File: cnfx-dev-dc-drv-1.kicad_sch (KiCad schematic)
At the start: 55 parts, among them J1 TC2030, J2 Conn_01x02, J3 Conn_01x04_Pin, J4 Conn_01x02, J7 Conn_01x03, J8 Conn_01x04_Pin, SW1 SW_Push, SW2 SW_Push, SW3 SW_Push, U1 SN65HVD230, U2 STM32F103C8Tx, U5 HT753-1, U6 TPS259472A, Y1 8M

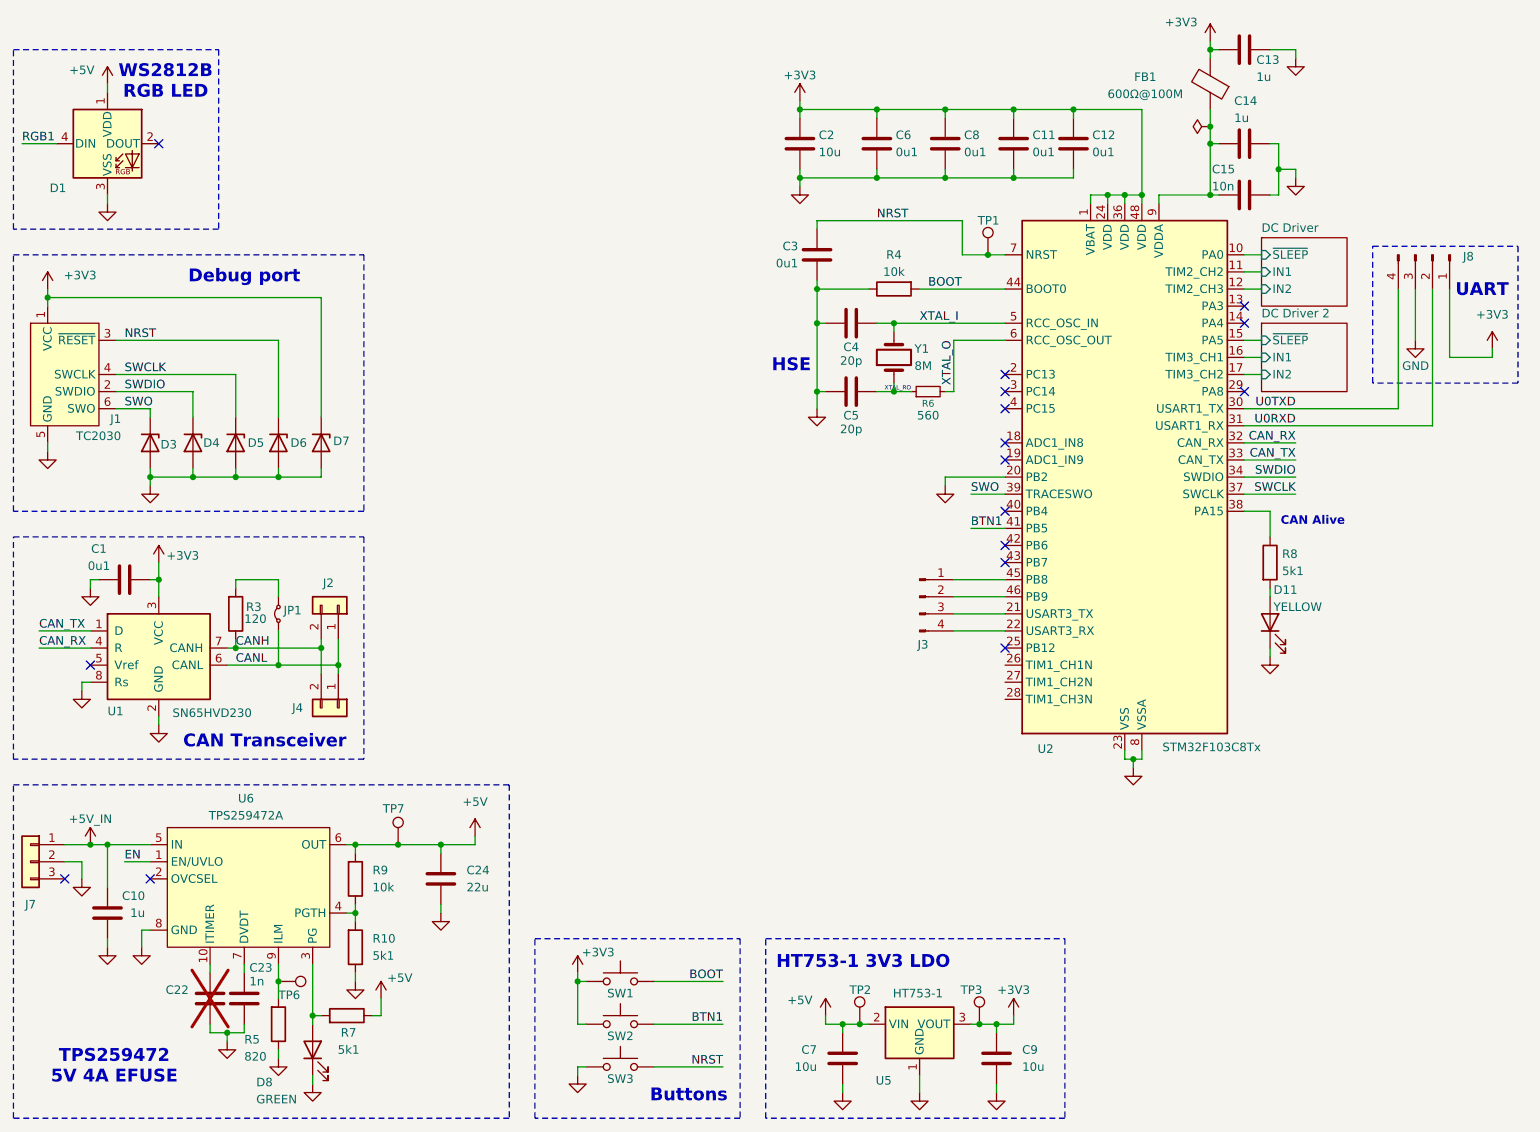
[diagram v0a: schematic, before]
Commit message: schem: connect rgb pin to stm32
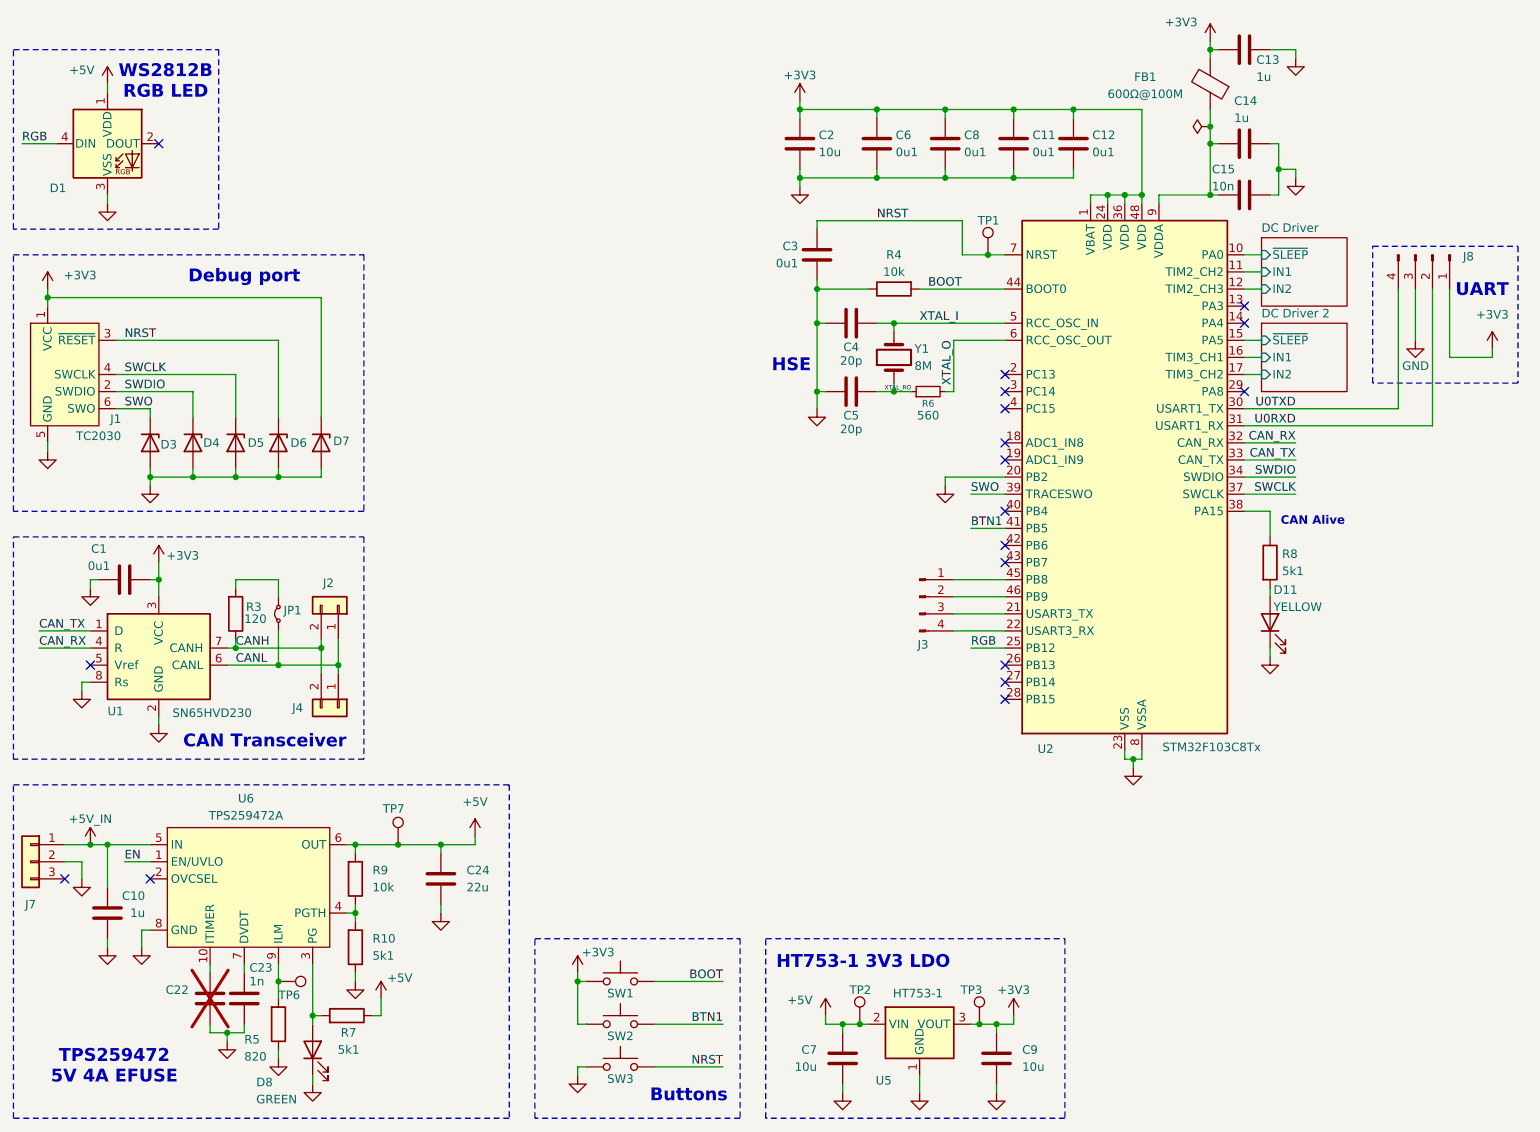
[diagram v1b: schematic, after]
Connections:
- net RGB1 is gone; now on net RGB: D1.4 (DIN)
- net RGB: now reaches U2.25 (PB12)
- no-connect marks 16 -> 18
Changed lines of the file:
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@@
 	)
 	(no_connect
+		(at 163.83 127)
+	)
+	(no_connect
 		(at 36.83 158.75)
 	)
@@
 	)
 	(no_connect
+		(at 163.83 129.54)
+	)
+	(no_connect
 		(at 163.83 93.98)
 	)
 	(no_connect
-		(at 163.83 124.46)
+		(at 163.83 132.08)
 	)
 	(no_connect
@@
 	(wire
 		(pts
+			(xy 158.75 124.46) (xy 163.83 124.46)
+		)
+		(stroke
+			(width 0)
+			(type default)
+		)
+	)
+	(wire
+		(pts
 			(xy 43.18 86.36) (xy 43.18 90.17)
 		)
@@
 		)
 	)
-	(label "RGB1"
+	(label "RGB"
 		(at 17.78 49.53 0)
 		(effects
@@
 		)
 	)
+	(label "RGB"
+		(at 158.75 124.46 0)
+		(effects
+			(font
+				(size 1.27 1.27)
+			)
+			(justify left bottom)
+		)
+	)
 	(label "NRST"
 		(at 144.78 60.96 0)
@@
 		)
 		(pin "27"
-			(alternate "TIM1_CH2N")
 		)
 		(pin "40"
@@
 		)
 		(pin "28"
-			(alternate "TIM1_CH3N")
 		)
 		(pin "30"
@@
 		)
 		(pin "26"
-			(alternate "TIM1_CH1N")
 		)
 		(pin "18"

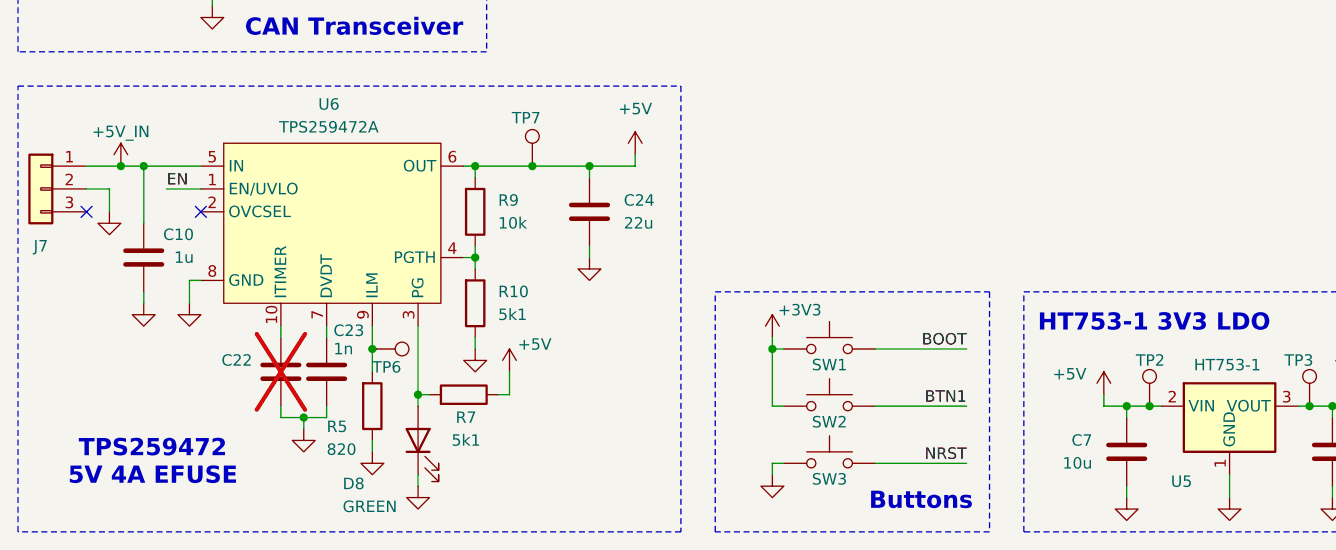
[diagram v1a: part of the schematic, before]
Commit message: schem: fix efuse en pin
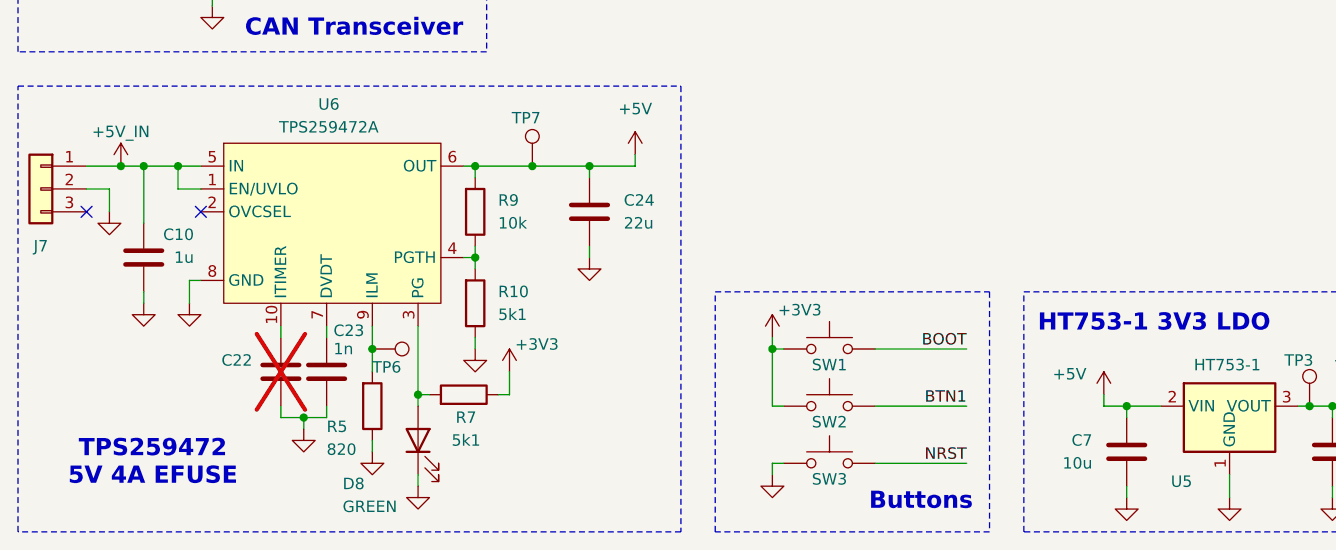
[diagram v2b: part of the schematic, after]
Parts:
- removed TP2: TestPoint, TestPoint:TestPoint_Pad_D2.0mm, symbol Connector:TestPoint
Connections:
- net EN is gone; now on net +5V_IN: U6.1 (EN/UVLO)
- net +3V3: now also R7.1
- net +5V: no longer R7.1
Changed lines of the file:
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@@
 	)
 	(junction
+		(at 34.29 153.67)
+		(diameter 0)
+		(color 0 0 0 0)
+	)
+	(junction
 		(at 62.23 124.46)
 		(diameter 0)
@@
 	)
 	(junction
-		(at 142.24 180.34)
-		(diameter 0)
-		(color 0 0 0 0)
-	)
-	(junction
 		(at 194.31 46.99)
 		(diameter 0)
@@
 	(wire
 		(pts
-			(xy 33.02 156.21) (xy 36.83 156.21)
-		)
-		(stroke
-			(width 0)
-			(type default)
-		)
-	)
-	(wire
-		(pts
 			(xy 195.58 57.15) (xy 194.31 57.15)
 		)
@@
 	(wire
 		(pts
+			(xy 34.29 156.21) (xy 34.29 153.67)
+		)
+		(stroke
+			(width 0)
+			(type default)
+		)
+	)
+	(wire
+		(pts
 			(xy 64.77 127) (xy 64.77 128.27)
 		)
@@
 	(wire
 		(pts
-			(xy 143.51 180.34) (xy 142.24 180.34)
-		)
-		(stroke
-			(width 0)
-			(type default)
-		)
-	)
-	(wire
-		(pts
 			(xy 30.48 153.67) (xy 30.48 160.02)
 		)
@@
 	(wire
 		(pts
+			(xy 34.29 156.21) (xy 36.83 156.21)
+		)
+		(stroke
+			(width 0)
+			(type default)
+		)
+	)
+	(wire
+		(pts
 			(xy 186.69 58.42) (xy 186.69 57.15)
 		)
@@
 	(wire
 		(pts
-			(xy 142.24 180.34) (xy 139.7 180.34)
+			(xy 139.7 180.34) (xy 143.51 180.34)
 		)
 		(stroke
@@
 	(wire
 		(pts
-			(xy 30.48 153.67) (xy 36.83 153.67)
+			(xy 30.48 153.67) (xy 34.29 153.67)
 		)
 		(stroke
@@
 	(wire
 		(pts
+			(xy 34.29 153.67) (xy 36.83 153.67)
+		)
+		(stroke
+			(width 0)
+			(type default)
+		)
+	)
+	(wire
+		(pts
 			(xy 207.01 93.98) (xy 199.39 93.98)
 		)
@@
 		)
 	)
-	(label "EN"
-		(at 33.02 156.21 0)
-		(effects
-			(font
-				(size 1.27 1.27)
-			)
-			(justify left bottom)
-		)
-	)
 	(label "CAN_RX"
 		(at 207.01 93.98 180)
@@
 	)
 	(symbol
+		(lib_id "power:+3V3")
+		(at 71.12 176.53 0)
+		(unit 1)
+		(body_style 1)
+		(exclude_from_sim no)
+		(in_bom yes)
+		(on_board yes)
+		(in_pos_files yes)
+		(dnp no)
+		(property "Reference" "#PWR044"
+			(at 71.12 180.34 0)
+			(hide yes)
+			(show_name no)
+			(do_not_autoplace no)
+			(effects
+				(font
+					(size 1.27 1.27)
+				)
+			)
+		)
+		(property "Value" "+3V3"
+			(at 74.168 173.482 0)
+			(show_name no)
+			(do_not_autoplace no)
+			(effects
+				(font
+					(size 1.27 1.27)
+				)
+			)
+		)
+		(property "Footprint" ""
+			(at 71.12 176.53 0)
+			(hide yes)
+			(show_name no)
+			(do_not_autoplace no)
+			(effects
+				(font
+					(size 1.27 1.27)
+				)
+			)
+		)
+		(property "Datasheet" ""
+			(at 71.12 176.53 0)
+			(hide yes)
+			(show_name no)
+			(do_not_autoplace no)
+			(effects
+				(font
+					(size 1.27 1.27)
+				)
+			)
+		)
+		(property "Description" "Power symbol creates a global label with name \"+3V3\""
+			(at 71.12 176.53 0)
+			(hide yes)
+			(show_name no)
+			(do_not_autoplace no)
+			(effects
+				(font
+					(size 1.27 1.27)
+				)
+			)
+		)
+		(pin "1"
+		)
+		(instances
+			(project "cnfx-dev-dc-drv-1"
+				(path "/d7250a19-615d-468e-abbc-0dea4b78aeef"
+					(reference "#PWR044")
+					(unit 1)
+				)
+			)
+		)
+	)
+	(symbol
 		(lib_id "power:GND")
 		(at 182.88 142.24 0)
@@
 	)
 	(symbol
-		(lib_id "Connector:TestPoint")
-		(at 142.24 180.34 0)
-		(unit 1)
-		(body_style 1)
-		(exclude_from_sim no)
-		(in_bom no)
-		(on_board yes)
-		(in_pos_files yes)
-		(dnp no)
-		(property "Reference" "TP2"
-			(at 140.716 175.26 0)
-			(show_name no)
-			(do_not_autoplace no)
-			(effects
-				(font
-					(size 1.27 1.27)
-				)
-				(justify left)
-			)
-		)
-		(property "Value" "TestPoint"
-			(at 144.78 178.3079 0)
-			(hide yes)
-			(show_name no)
-			(do_not_autoplace no)
-			(effects
-				(font
-					(size 1.27 1.27)
-				)
-				(justify left)
-			)
-		)
-		(property "Footprint" "TestPoint:TestPoint_Pad_D2.0mm"
-			(at 147.32 180.34 0)
-			(hide yes)
-			(show_name no)
-			(do_not_autoplace no)
-			(effects
-				(font
-					(size 1.27 1.27)
-				)
-			)
-		)
-		(property "Datasheet" ""
-			(at 147.32 180.34 0)
-			(hide yes)
-			(show_name no)
-			(do_not_autoplace no)
-			(effects
-				(font
-					(size 1.27 1.27)
-				)
-			)
-		)
-		(property "Description" "test point"
-			(at 142.24 180.34 0)
-			(hide yes)
-			(show_name no)
-			(do_not_autoplace no)
-			(effects
-				(font
-					(size 1.27 1.27)
-				)
-			)
-		)
-		(pin "1"
-		)
-		(instances
-			(project "cnfx-dev-dc-drv-1"
-				(path "/d7250a19-615d-468e-abbc-0dea4b78aeef"
-					(reference "TP2")
-					(unit 1)
-				)
-			)
-		)
-	)
-	(symbol
 		(lib_id "Connector:Conn_01x04_Pin")
 		(at 227.33 66.04 270)
@@
 					(unit 1)
 				)
-			)
-		)
-	)
-	(symbol
-		(lib_id "power:VBUS")
-		(at 71.12 176.53 0)
-		(unit 1)
-		(body_style 1)
-		(exclude_from_sim no)
-		(in_bom yes)
-		(on_board yes)
-		(in_pos_files yes)
-		(dnp no)
-		(property "Reference" "#PWR044"
-			(at 71.12 180.34 0)
-			(hide yes)
-			(show_name no)
-			(do_not_autoplace no)
-			(effects
-				(font
-					(size 1.27 1.27)
-				)
-			)
-		)
-		(property "Value" "+5V"
-			(at 73.914 173.482 0)
-			(show_name no)
-			(do_not_autoplace no)
-			(effects
-				(font
-					(size 1.27 1.27)
-				)
-			)
-		)
-		(property "Footprint" ""
-			(at 71.12 176.53 0)
-			(hide yes)
-			(show_name no)
-			(do_not_autoplace no)
-			(effects
-				(font
-					(size 1.27 1.27)
-				)
-			)
-		)
-		(property "Datasheet" ""
-			(at 71.12 176.53 0)
-			(hide yes)
-			(show_name no)
-			(do_not_autoplace no)
-			(effects
-				(font
-					(size 1.27 1.27)
-				)
-			)
-		)
-		(property "Description" "Power symbol creates a global label with name \"VBUS\""
-			(at 71.12 176.53 0)
-			(hide yes)
-			(show_name no)
-			(do_not_autoplace no)
-			(effects
-				(font
-					(size 1.27 1.27)
-				)
-			)
-		)
-		(pin "1"
-		)
-		(instances
-			(project "cnfx-dev-dc-drv-1"
-				(path "/d7250a19-615d-468e-abbc-0dea4b78aeef"
-					(reference "#PWR044")
-					(unit 1)
-				)

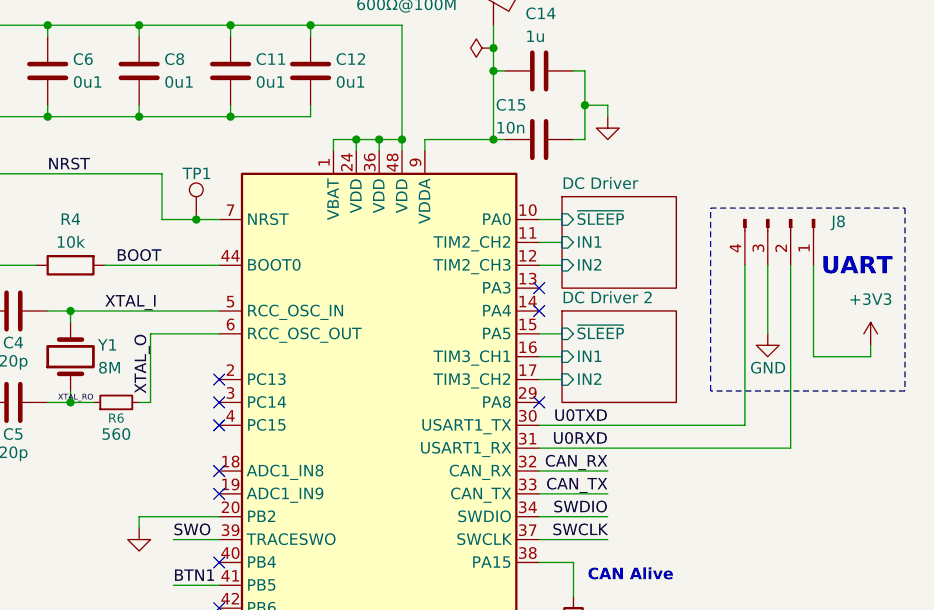
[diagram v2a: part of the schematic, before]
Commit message: schem: add test points
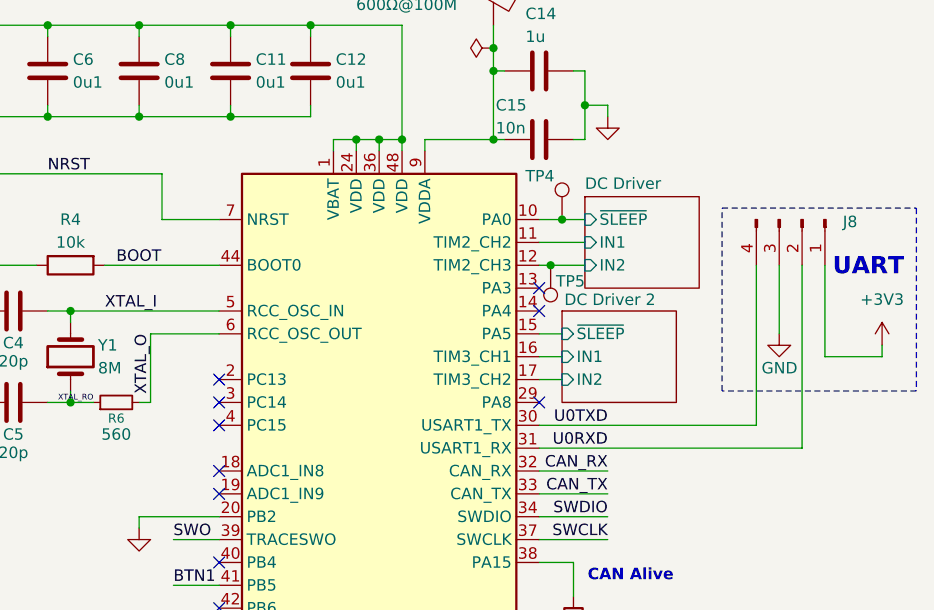
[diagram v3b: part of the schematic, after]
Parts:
- removed TP1: TestPoint, TestPoint:TestPoint_Pad_D2.0mm, symbol Connector:TestPoint
- added TP4, TP5: TestPoint, TestPoint:TestPoint_Pad_D2.0mm, symbol Connector:TestPoint
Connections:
- net DC Driver/IN2: now also TP5.1
- net DC Driver/~{SLEEP}: now also TP4.1
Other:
- moved on the sheet: J8
